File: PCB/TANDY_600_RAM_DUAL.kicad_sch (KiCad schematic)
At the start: 6 parts, among them J1 TANDY_600_RAM_DUAL, U1 AS6C4008_TSOP-I_sTSOP, U2 74HC148, U3 74LVC1G02

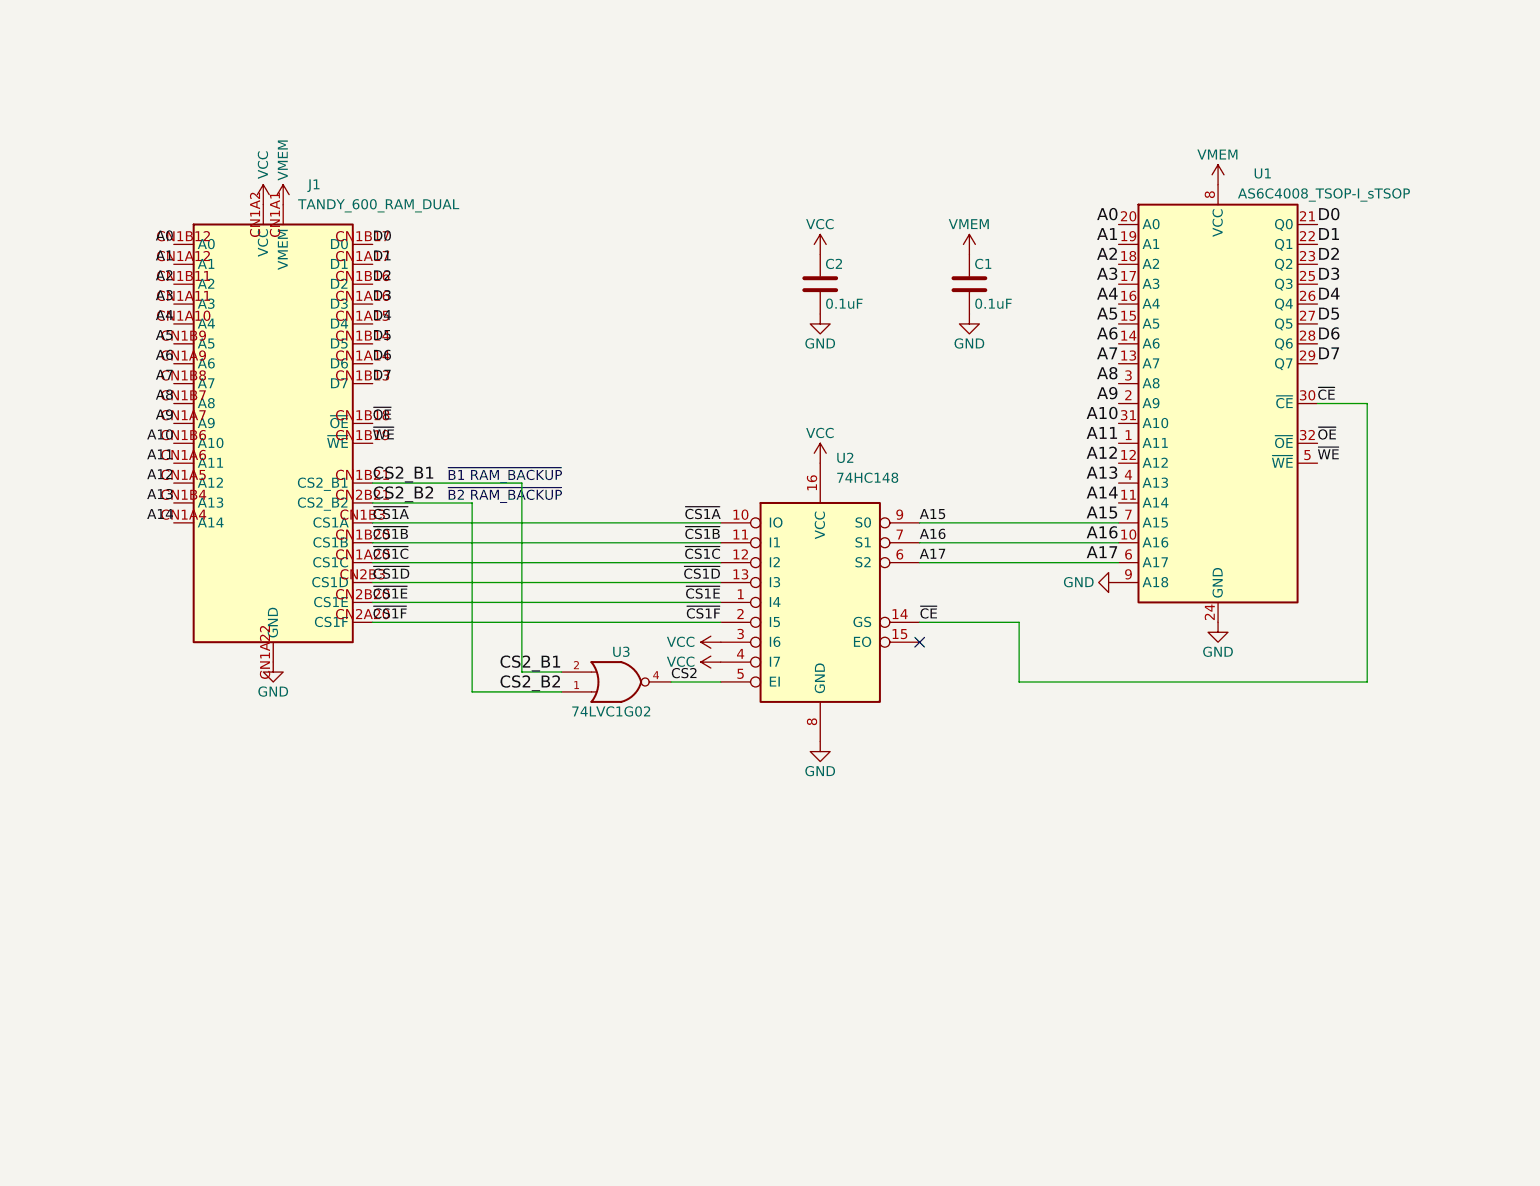
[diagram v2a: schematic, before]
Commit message: gnd on tiny, new dual sch, bus connector symbol & footprint
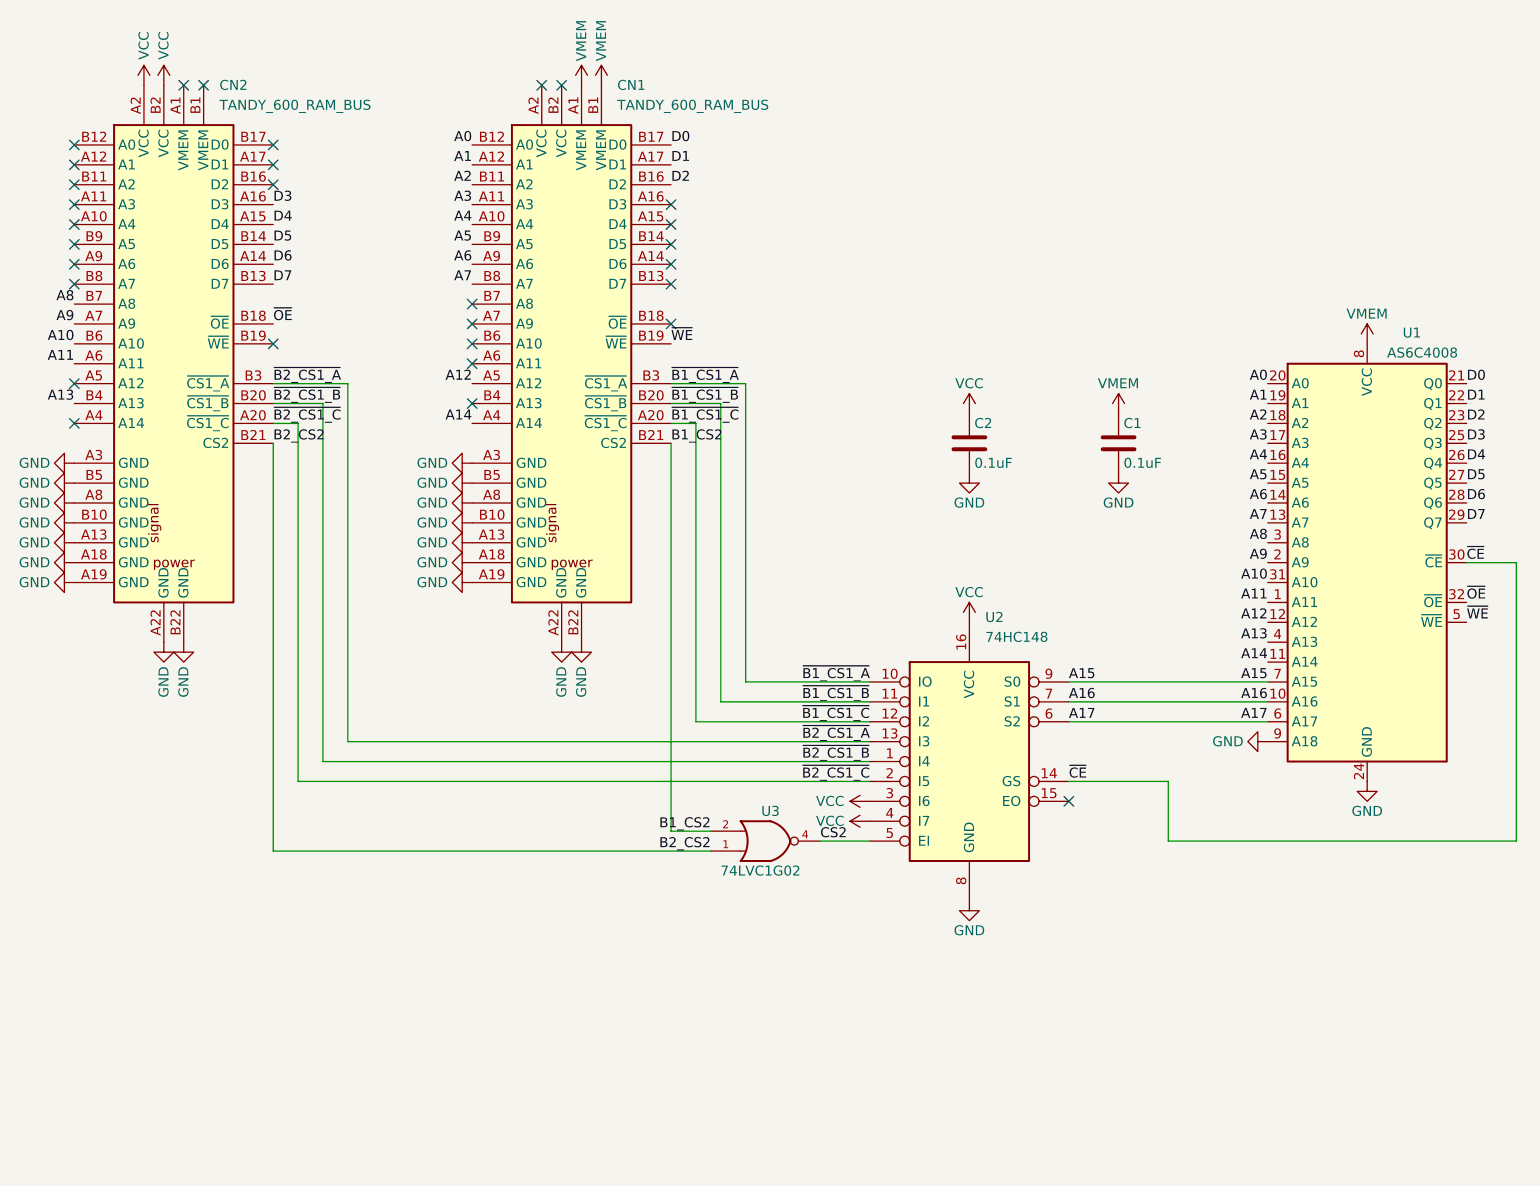
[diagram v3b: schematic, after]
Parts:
- removed J1: TANDY_600_RAM_DUAL, 000_LOCAL:TANDY_600_RAM_DUAL, symbol 000_LOCAL:TANDY_600_RAM_DUAL
- added CN1, CN2: TANDY_600_RAM_BUS, 000_LOCAL:DIN41612-2x22_male_vertical, symbol 000_LOCAL:TANDY_600_RAM_BUS_plain_pins
- U1: value AS6C4008_TSOP-I_sTSOP -> AS6C4008
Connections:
- net A0: now also CN1.B12 (A0)
- net A1: now also CN1.A12 (A1)
- net A10: now also CN2.B6 (A10)
- net A11: now also CN2.A6 (A11)
- net A12: now also CN1.A5 (A12)
- net A13: now also CN2.B4 (A13)
- net A14: now also CN1.A4 (A14)
- net A2: now also CN1.B11 (A2)
- net A3: now also CN1.A11 (A3)
- net A4: now also CN1.A10 (A4)
- net A5: now also CN1.B9 (A5)
- net A6: now also CN1.A9 (A6)
- net A7: now also CN1.B8 (A7)
- net A8: now also CN2.B7 (A8)
- net A9: now also CN2.A7 (A9)
- net D0: now also CN1.B17 (D0)
- net D1: now also CN1.A17 (D1)
- net D2: now also CN1.B16 (D2)
- net D3: now also CN2.A16 (D3)
- net D4: now also CN2.A15 (D4)
- net D5: now also CN2.B14 (D5)
- net D6: now also CN2.A14 (D6)
- net D7: now also CN2.B13 (D7)
- net GND: now also CN1.A13 (GND), CN1.A18 (GND), CN1.A19 (GND), CN1.A22 (GND), CN1.A3 (GND), CN1.A8 (GND), CN1.B10 (GND), CN1.B22 (GND), CN1.B5 (GND), CN2.A13 (GND), CN2.A18 (GND), CN2.A19 (GND), CN2.A22 (GND), CN2.A3 (GND), CN2.A8 (GND), CN2.B10 (GND), CN2.B22 (GND), CN2.B5 (GND)
- net VCC: now also CN2.A2 (VCC), CN2.B2 (VCC)
- net VMEM: now also CN1.A1 (VMEM), CN1.B1 (VMEM)
- net ~{OE}: now also CN2.B18 (~{OE})
- net ~{WE}: now also CN1.B19 (~{WE})
- net CS2_B1 renamed B1_CS2
- net B1_CS2: now also CN1.B21 (CS2)
- net CS2_B2 renamed B2_CS2
- net B2_CS2: now also CN2.B21 (CS2)
- net ~{CS1A} renamed ~{B1_CS1_A}
- net ~{B1_CS1_A}: now also CN1.B3 (~{CS1_A})
- net ~{CS1B} renamed ~{B1_CS1_B}
- net ~{B1_CS1_B}: now also CN1.B20 (~{CS1_B})
- net ~{CS1C} renamed ~{B1_CS1_C}
- net ~{B1_CS1_C}: now also CN1.A20 (~{CS1_C})
- net ~{CS1D} renamed ~{B2_CS1_A}
- net ~{B2_CS1_A}: now also CN2.B3 (~{CS1_A})
- net ~{CS1E} renamed ~{B2_CS1_B}
- net ~{B2_CS1_B}: now also CN2.B20 (~{CS1_B})
- net ~{CS1F} renamed ~{B2_CS1_C}
- net ~{B2_CS1_C}: now also CN2.A20 (~{CS1_C})
- no-connect marks 1 -> 30
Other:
- note removed: "~{B1 RAM_BACKUP}"
- note removed: "~{B2 RAM_BACKUP}"
- title: TANDY 600 DUAL RAM -> TANDY 600 RAM
- moved on the sheet: C1, C2, U1, U2, U3
